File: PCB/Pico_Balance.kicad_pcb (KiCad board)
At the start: 2 copper layers, 100 x 52 mm, 42 parts, among them J1 XT60PW-M, J2 GPIO_Ext, J3 Conn_Motor0, J4 Conn_Motor1, J5 5V3A OUT, Q1 CSD17577Q3A, U1 BMI160, U2 DRV8876PWPR, U3 DRV8876PWPR, U4 LM74610QDGKRQ1, U5 LMR51430

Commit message: Refinements
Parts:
- U1: value BMI160 -> BMI323
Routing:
- net +3V3: track 200.9 -> 210.2 mm, vias 2 -> 3
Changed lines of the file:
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@@
 			)
 		)
-		(property "Value" "BMI160"
+		(property "Value" "BMI323"
 			(at 4.3375 0.45 270)
 			(unlocked yes)
@@
 		(embedded_fonts no)
 	)
+	(gr_line
+		(start 249 80)
+		(end 248.25 80.5)
+		(stroke
+			(width 0.2)
+			(type solid)
+		)
+		(layer "F.SilkS")
+	)
 	(gr_rect
 		(start 155.8 73)
@@
 		(layer "F.SilkS")
 	)
+	(gr_line
+		(start 245 80)
+		(end 249 80)
+		(stroke
+			(width 0.2)
+			(type solid)
+		)
+		(layer "F.SilkS")
+	)
 	(gr_rect
 		(start 155.8 114.6)
@@
 		(layer "F.SilkS")
 	)
+	(gr_line
+		(start 249 80)
+		(end 248.25 79.5)
+		(stroke
+			(width 0.2)
+			(type solid)
+		)
+		(layer "F.SilkS")
+	)
+	(gr_line
+		(start 245 76)
+		(end 245.5 76.75)
+		(stroke
+			(width 0.2)
+			(type solid)
+		)
+		(layer "F.SilkS")
+	)
+	(gr_circle
+		(center 245 80)
+		(end 245.5 80)
+		(stroke
+			(width 0.2)
+			(type solid)
+		)
+		(fill no)
+		(layer "F.SilkS")
+	)
+	(gr_line
+		(start 245 76)
+		(end 244.5 76.75)
+		(stroke
+			(width 0.2)
+			(type solid)
+		)
+		(layer "F.SilkS")
+	)
 	(gr_rect
 		(start 242.6 83.6)
-		(end 251 90.4)
+		(end 251 90.5)
 		(stroke
 			(width 0.2)
@@
 		(layer "F.SilkS")
 	)
+	(gr_line
+		(start 245 80)
+		(end 245 76)
+		(stroke
+			(width 0.2)
+			(type solid)
+		)
+		(layer "F.SilkS")
+	)
 	(gr_rect
 		(start 200.725 120.8)
@@
 		(cells
 			(table_cell "M+"
-				(start 171.95 73.25)
-				(end 169.3 76.8)
+				(start 171.95 73.725)
+				(end 169.3 77.275)
 				(margins 0.1 0.1 0.1 0.1)
 				(span 1 1)
@@
 						(thickness 0.15)
 					)
-					(justify left)
 				)
 			)
 			(table_cell "3V"
-				(start 169.3 73.25)
-				(end 166.8 76.8)
+				(start 169.3 73.725)
+				(end 166.8 77.275)
 				(margins 0.1 0.1 0.1 0.1)
 				(span 1 1)
@@
 						(thickness 0.15)
 					)
-					(justify left)
 				)
 			)
 			(table_cell "EA"
-				(start 166.8 73.25)
-				(end 164.4 76.8)
+				(start 166.8 73.725)
+				(end 164.4 77.275)
 				(margins 0.1 0.1 0.1 0.1)
 				(span 1 1)
@@
 						(thickness 0.15)
 					)
-					(justify left)
 				)
 			)
 			(table_cell "EB"
-				(start 164.4 73.25)
-				(end 161.6 76.8)
+				(start 164.4 73.725)
+				(end 161.6 77.275)
 				(margins 0.1 0.1 0.1 0.1)
 				(span 1 1)
@@
 						(thickness 0.15)
 					)
-					(justify left)
 				)
 			)
 			(table_cell "GND"
-				(start 161.6 73.25)
-				(end 159.4 76.8)
+				(start 161.6 73.725)
+				(end 159.4 77.275)
 				(margins 0.1 0.1 0.1 0.1)
 				(span 1 1)
@@
 						(thickness 0.15)
 					)
-					(justify left)
 				)
 			)
 			(table_cell "M-"
-				(start 159.4 73.25)
-				(end 156.8 76.8)
+				(start 159.4 73.725)
+				(end 156.8 77.275)
 				(margins 0.1 0.1 0.1 0.1)
 				(span 1 1)
@@
 						(thickness 0.15)
 					)
-					(justify left)
 				)
 			)
@@
 		(cells
 			(table_cell "M+"
-				(start 171.975 119.425)
-				(end 169.325 122.975)
+				(start 171.975 118.725)
+				(end 169.325 122.275)
 				(margins 0.1 0.1 0.1 0.1)
 				(span 1 1)
@@
 						(thickness 0.15)
 					)
-					(justify left)
 				)
 			)
 			(table_cell "3V"
-				(start 169.325 119.425)
-				(end 166.825 122.975)
+				(start 169.325 118.725)
+				(end 166.825 122.275)
 				(margins 0.1 0.1 0.1 0.1)
 				(span 1 1)
@@
 						(thickness 0.15)
 					)
-					(justify left)
 				)
 			)
 			(table_cell "EA"
-				(start 166.825 119.425)
-				(end 164.425 122.975)
+				(start 166.825 118.725)
+				(end 164.425 122.275)
 				(margins 0.1 0.1 0.1 0.1)
 				(span 1 1)
@@
 						(thickness 0.15)
 					)
-					(justify left)
 				)
 			)
 			(table_cell "EB"
-				(start 164.425 119.425)
-				(end 161.625 122.975)
+				(start 164.425 118.725)
+				(end 161.625 122.275)
 				(margins 0.1 0.1 0.1 0.1)
 				(span 1 1)
@@
 						(thickness 0.15)
 					)
-					(justify left)
 				)
 			)
 			(table_cell "GND"
-				(start 161.625 119.425)
-				(end 159.425 122.975)
+				(start 161.625 118.725)
+				(end 159.425 122.275)
 				(margins 0.1 0.1 0.1 0.1)
 				(span 1 1)
@@
 						(thickness 0.15)
 					)
-					(justify left)
 				)
 			)
 			(table_cell "M-"
-				(start 159.425 119.425)
-				(end 156.825 122.975)
+				(start 159.425 118.725)
+				(end 156.825 122.275)
 				(margins 0.1 0.1 0.1 0.1)
 				(span 1 1)
@@
 						(thickness 0.15)
 					)
-					(justify left)
 				)
 			)
@@
 	)
 	(segment
+		(start 243.4 88.4)
+		(end 242.848527 88.4)
+		(width 0.2)
+		(layer "F.Cu")
+		(net 9)
+	)
+	(segment
 		(start 219.001 72.601)
 		(end 174.599 72.601)
@@
 	)
 	(segment
+		(start 242.848527 88.4)
+		(end 242.048527 87.6)
+		(width 0.2)
+		(layer "F.Cu")
+		(net 9)
+	)
+	(segment
 		(start 245.1625 87.7175)
 		(end 245.1625 87.5625)
@@
 	)
 	(segment
+		(start 243.4 88.4)
+		(end 243.4 86.2355)
+		(width 0.2)
+		(layer "F.Cu")
+		(net 9)
+	)
+	(segment
 		(start 162.539 82.611)
 		(end 160.7 84.45)
@@
 	(segment
 		(start 243.4 89.48)
-		(end 243.4 86.2355)
+		(end 243.4 88.4)
 		(width 0.2)
 		(layer "F.Cu")
@@
 	)
 	(via
+		(at 242.048527 87.6)
+		(size 0.6)
+		(drill 0.3)
+		(layers "F.Cu" "B.Cu")
+		(net 9)
+	)
+	(via
 		(at 153.602 92.6)
 		(size 0.6)
@@
 	)
 	(segment
+		(start 238.648527 84.2)
+		(end 235.865 84.2)
+		(width 0.2)
+		(layer "B.Cu")
+		(net 9)
+	)
+	(segment
+		(start 242.048527 87.6)
+		(end 238.648527 84.2)
+		(width 0.2)
+		(layer "B.Cu")
+		(net 9)
+	)
+	(segment
 		(start 153.602 112.202)
 		(end 153.602 109.8)
@@
 	)
 	(segment
-		(start 246.789 94.389)
-		(end 240.6 88.2)
+		(start 244.601 103.601)
+		(end 244.601 92.201)
 		(width 0.2)
 		(layer "B.Cu")
@@
 	)
 	(segment
-		(start 245.6 86.4)
-		(end 243.8 88.2)
+		(start 247.94 119.28)
+		(end 246.789 118.129)
 		(width 0.2)
 		(layer "B.Cu")
@@
 	)
 	(segment
-		(start 246.789 118.129)
-		(end 246.789 94.389)
+		(start 245.6 86.4)
+		(end 243.8 88.2)
 		(width 0.2)
 		(layer "B.Cu")
@@
 	)
 	(segment
-		(start 247.94 119.28)
-		(end 246.789 118.129)
+		(start 244.601 92.201)
+		(end 240.6 88.2)
 		(width 0.2)
 		(layer "B.Cu")
@@
 	)
 	(segment
+		(start 246.789 105.789)
+		(end 244.601 103.601)
+		(width 0.2)
+		(layer "B.Cu")
+		(net 18)
+	)
+	(segment
 		(start 219.186 88.179)
 		(end 218.085 89.28)
@@
 	)
 	(segment
+		(start 246.789 118.129)
+		(end 246.789 105.789)
+		(width 0.2)
+		(layer "B.Cu")
+		(net 18)
+	)
+	(segment
 		(start 173.098 122.3)
 		(end 173 122.398)
@@
 	)
 	(group ""
+		(members "0e098a54-aab8-48f0-ad5a-1b8c5dcb6939" "3d4db691-04d1-4923-84a8-ca63cf973a07"
+			"4c652e14-a829-45d9-ae98-6ccd60f11574" "63e503f4-efba-4b57-b139-408cbbdc4a5a"
+			"90350472-ea7e-46d9-adf6-18d1887b5930" "97e5d2a3-c56d-46de-99b1-c52cc26e95a4"
+			"af4be8ed-c6e8-495a-9d4b-11de16a7dfe8"
+		)
+	)
+	(group ""

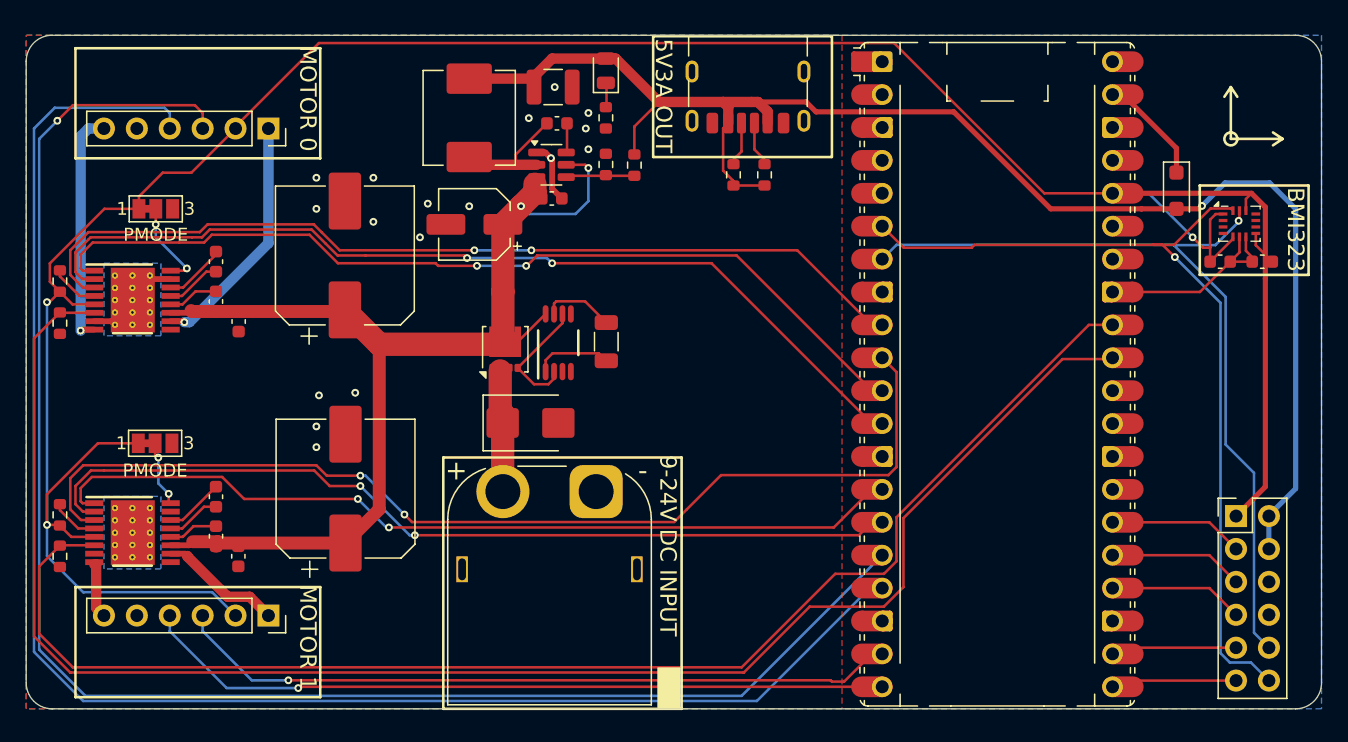
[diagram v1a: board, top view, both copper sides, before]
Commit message: minor silkscreen and drc error correction
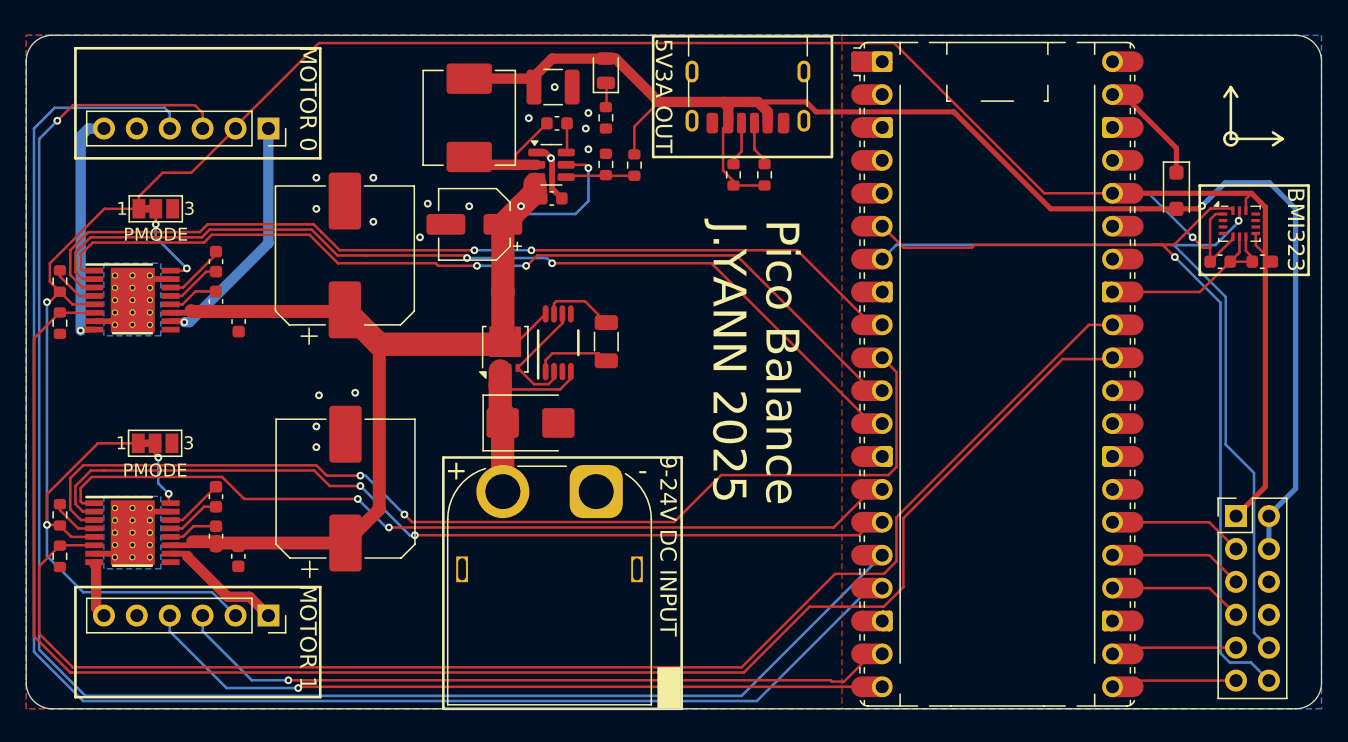
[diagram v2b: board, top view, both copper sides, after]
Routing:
- net Net-(D1-A1): track 9.41 -> 15.9 mm
- net GND: track 24.4 -> 27.8 mm
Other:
- board text added: "Pico Balance J.YANN 2025"
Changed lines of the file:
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@@
 		(pad "1" smd roundrect
 			(at -1.44 -0.97 90)
-			(size 0.63 0.5)
+			(size 0.63 0.33)
 			(layers "F.Cu" "F.Mask" "F.Paste")
 			(roundrect_rratio 0.25)
@@
 		(pad "2" smd roundrect
 			(at -1.44 -0.33 90)
-			(size 0.63 0.5)
+			(size 0.63 0.33)
 			(layers "F.Cu" "F.Mask" "F.Paste")
 			(roundrect_rratio 0.25)
@@
 		(pad "3" smd roundrect
 			(at -1.44 0.33 90)
-			(size 0.63 0.5)
+			(size 0.63 0.33)
 			(layers "F.Cu" "F.Mask" "F.Paste")
 			(roundrect_rratio 0.25)
@@
 		(pad "4" smd roundrect
 			(at -1.44 0.97 90)
-			(size 0.63 0.5)
+			(size 0.63 0.33)
 			(layers "F.Cu" "F.Mask" "F.Paste")
 			(roundrect_rratio 0.25)
@@
 		(pad "17" thru_hole circle
 			(at -1.35 -1.900001)
-			(size 0.499999 0.499999)
-			(drill 0.2032)
+			(size 0.5 0.5)
+			(drill 0.3)
 			(layers "*.Cu" "*.Mask")
 			(remove_unused_layers no)
@@
 		(pad "17" thru_hole circle
 			(at -1.35 -0.950001)
-			(size 0.499999 0.499999)
-			(drill 0.2032)
+			(size 0.5 0.5)
+			(drill 0.3)
 			(layers "*.Cu" "*.Mask")
 			(remove_unused_layers no)
@@
 		(pad "17" thru_hole circle
 			(at -1.35 0)
-			(size 0.499999 0.499999)
-			(drill 0.2032)
+			(size 0.5 0.5)
+			(drill 0.3)
 			(layers "*.Cu" "*.Mask")
 			(remove_unused_layers no)
@@
 		(pad "17" thru_hole circle
 			(at -1.35 0.950001)
-			(size 0.499999 0.499999)
-			(drill 0.2032)
+			(size 0.5 0.5)
+			(drill 0.3)
 			(layers "*.Cu" "*.Mask")
 			(remove_unused_layers no)
@@
 		(pad "17" thru_hole circle
 			(at -1.35 1.900001)
-			(size 0.499999 0.499999)
-			(drill 0.2032)
+			(size 0.5 0.5)
+			(drill 0.3)
 			(layers "*.Cu" "*.Mask")
 			(remove_unused_layers no)
@@
 		(pad "17" thru_hole circle
 			(at 0 -1.900001)
-			(size 0.499999 0.499999)
-			(drill 0.2032)
+			(size 0.5 0.5)
+			(drill 0.3)
 			(layers "*.Cu" "*.Mask")
 			(remove_unused_layers no)
@@
 		(pad "17" thru_hole circle
 			(at 0 -0.950001)
-			(size 0.499999 0.499999)
-			(drill 0.2032)
+			(size 0.5 0.5)
+			(drill 0.3)
 			(layers "*.Cu" "*.Mask")
 			(remove_unused_layers no)
@@
 		(pad "17" thru_hole circle
 			(at 0 0)
-			(size 0.499999 0.499999)
-			(drill 0.2032)
+			(size 0.5 0.5)
+			(drill 0.3)
 			(layers "*.Cu" "*.Mask")
 			(remove_unused_layers no)
@@
 		(pad "17" thru_hole circle
 			(at 0 0.950001)
-			(size 0.499999 0.499999)
-			(drill 0.2032)
+			(size 0.5 0.5)
+			(drill 0.3)
 			(layers "*.Cu" "*.Mask")
 			(remove_unused_layers no)
@@
 		(pad "17" thru_hole circle
 			(at 0 1.900001)
-			(size 0.499999 0.499999)
-			(drill 0.2032)
+			(size 0.5 0.5)
+			(drill 0.3)
 			(layers "*.Cu" "*.Mask")
 			(remove_unused_layers no)
@@
 		(pad "17" thru_hole circle
 			(at 1.35 -1.900001)
-			(size 0.499999 0.499999)
-			(drill 0.2032)
+			(size 0.5 0.5)
+			(drill 0.3)
 			(layers "*.Cu" "*.Mask")
 			(remove_unused_layers no)
@@
 		(pad "17" thru_hole circle
 			(at 1.35 -0.950001)
-			(size 0.499999 0.499999)
-			(drill 0.2032)
+			(size 0.5 0.5)
+			(drill 0.3)
 			(layers "*.Cu" "*.Mask")
 			(remove_unused_layers no)
@@
 		(pad "17" thru_hole circle
 			(at 1.35 0)
-			(size 0.499999 0.499999)
-			(drill 0.2032)
+			(size 0.5 0.5)
+			(drill 0.3)
 			(layers "*.Cu" "*.Mask")
 			(remove_unused_layers no)
@@
 		(pad "17" thru_hole circle
 			(at 1.35 0.950001)
-			(size 0.499999 0.499999)
-			(drill 0.2032)
+			(size 0.5 0.5)
+			(drill 0.3)
 			(layers "*.Cu" "*.Mask")
 			(remove_unused_layers no)
@@
 		(pad "17" thru_hole circle
 			(at 1.35 1.900001)
-			(size 0.499999 0.499999)
-			(drill 0.2032)
+			(size 0.5 0.5)
+			(drill 0.3)
 			(layers "*.Cu" "*.Mask")
 			(remove_unused_layers no)
@@
 		(pad "17" thru_hole circle
 			(at -1.35 -1.900001)
-			(size 0.499999 0.499999)
-			(drill 0.2032)
+			(size 0.5 0.5)
+			(drill 0.3)
 			(layers "*.Cu" "*.Mask")
 			(remove_unused_layers no)
@@
 		(pad "17" thru_hole circle
 			(at -1.35 -0.950001)
-			(size 0.499999 0.499999)
-			(drill 0.2032)
+			(size 0.5 0.5)
+			(drill 0.3)
 			(layers "*.Cu" "*.Mask")
 			(remove_unused_layers no)
@@
 		(pad "17" thru_hole circle
 			(at -1.35 0)
-			(size 0.499999 0.499999)
-			(drill 0.2032)
+			(size 0.5 0.5)
+			(drill 0.3)
 			(layers "*.Cu" "*.Mask")
 			(remove_unused_layers no)
@@
 		(pad "17" thru_hole circle
 			(at -1.35 0.950001)
-			(size 0.499999 0.499999)
-			(drill 0.2032)
+			(size 0.5 0.5)
+			(drill 0.3)
 			(layers "*.Cu" "*.Mask")
 			(remove_unused_layers no)
@@
 		(pad "17" thru_hole circle
 			(at -1.35 1.900001)
-			(size 0.499999 0.499999)
-			(drill 0.2032)
+			(size 0.5 0.5)
+			(drill 0.3)
 			(layers "*.Cu" "*.Mask")
 			(remove_unused_layers no)
@@
 		(pad "17" thru_hole circle
 			(at 0 -1.900001)
-			(size 0.499999 0.499999)
-			(drill 0.2032)
+			(size 0.5 0.5)
+			(drill 0.3)
 			(layers "*.Cu" "*.Mask")
 			(remove_unused_layers no)
@@
 		(pad "17" thru_hole circle
 			(at 0 -0.950001)
-			(size 0.499999 0.499999)
-			(drill 0.2032)
+			(size 0.5 0.5)
+			(drill 0.3)
 			(layers "*.Cu" "*.Mask")
 			(remove_unused_layers no)
@@
 		(pad "17" thru_hole circle
 			(at 0 0)
-			(size 0.499999 0.499999)
-			(drill 0.2032)
+			(size 0.5 0.5)
+			(drill 0.3)
 			(layers "*.Cu" "*.Mask")
 			(remove_unused_layers no)
@@
 		(pad "17" thru_hole circle
 			(at 0 0.950001)
-			(size 0.499999 0.499999)
-			(drill 0.2032)
+			(size 0.5 0.5)
+			(drill 0.3)
 			(layers "*.Cu" "*.Mask")
 			(remove_unused_layers no)
@@
 		(pad "17" thru_hole circle
 			(at 0 1.900001)
-			(size 0.499999 0.499999)
-			(drill 0.2032)
+			(size 0.5 0.5)
+			(drill 0.3)
 			(layers "*.Cu" "*.Mask")
 			(remove_unused_layers no)
@@
 		(pad "17" thru_hole circle
 			(at 1.35 -1.900001)
-			(size 0.499999 0.499999)
-			(drill 0.2032)
+			(size 0.5 0.5)
+			(drill 0.3)
 			(layers "*.Cu" "*.Mask")
 			(remove_unused_layers no)
@@
 		(pad "17" thru_hole circle
 			(at 1.35 -0.950001)
-			(size 0.499999 0.499999)
-			(drill 0.2032)
+			(size 0.5 0.5)
+			(drill 0.3)
 			(layers "*.Cu" "*.Mask")
 			(remove_unused_layers no)
@@
 		(pad "17" thru_hole circle
 			(at 1.35 0)
-			(size 0.499999 0.499999)
-			(drill 0.2032)
+			(size 0.5 0.5)
+			(drill 0.3)
 			(layers "*.Cu" "*.Mask")
 			(remove_unused_layers no)
@@
 		(pad "17" thru_hole circle
 			(at 1.35 0.950001)
-			(size 0.499999 0.499999)
-			(drill 0.2032)
+			(size 0.5 0.5)
+			(drill 0.3)
 			(layers "*.Cu" "*.Mask")
 			(remove_unused_layers no)
@@
 		(pad "17" thru_hole circle
 			(at 1.35 1.900001)
-			(size 0.499999 0.499999)
-			(drill 0.2032)
+			(size 0.5 0.5)
+			(drill 0.3)
 			(layers "*.Cu" "*.Mask")
 			(remove_unused_layers no)
@@
 		(layer "Edge.Cuts")
 	)
+	(gr_text "Pico Balance\nJ.YANN 2025"
+		(at 204.75 97.25 270)
+		(layer "F.SilkS" knockout)
+		(effects
+			(font
+				(size 2.54 2.54)
+				(thickness 0.4)
+			)
+			(justify bottom)
+		)
+	)
 	(gr_text "MOTOR 1"
 		(at 173 114.4 270)
@@
 	)
 	(segment
+		(start 163.150002 108.775002)
+		(end 161.825003 108.775002)
+		(width 0.45)
+		(layer "F.Cu")
+		(net 8)
+	)
+	(segment
+		(start 158.575 112.025001)
+		(end 158.85 112.300001)
+		(width 0.45)
+		(layer "F.Cu")
+		(net 8)
+	)
+	(segment
 		(start 246.65 89.13)
 		(end 246.1625 88.6425)
@@
 	)
 	(segment
+		(start 157.250001 112.025001)
+		(end 158.575 112.025001)
+		(width 0.45)
+		(layer "F.Cu")
+		(net 8)
+	)
+	(segment
 		(start 194.15 76)
 		(end 194.15 76.75)
@@
 	)
 	(segment
+		(start 161.825003 108.775002)
+		(end 161.55 108.499999)
+		(width 0.45)
+		(layer "F.Cu")
+		(net 8)
+	)
+	(segment
 		(start 244.95 89.48)
 		(end 242.61 91.82)
@@
 	)
 	(segment
+		(start 193.214377 99.341999)
+		(end 188.933499 99.341999)
+		(width 0.2)
+		(layer "F.Cu")
+		(net 55)
+	)
+	(segment
 		(start 188.8 105.5975)
 		(end 188.8 107.23)
@@
 	(segment
 		(start 188.5915 100.9915)
-		(end 188.5915 97.911)
+		(end 188.5915 99)
 		(width 1.8)
 		(layer "F.Cu")
@@
 		(layer "F.Cu")
 		(net 55)
+	)
+	(segment
+		(start 188.5915 99)
+		(end 188.5915 97.911)
+		(width 1.8)
+		(layer "F.Cu")
+		(net 55)
+	)
+	(segment
+		(start 194.047502 97.964999)
+		(end 194.047502 98.508874)
+		(width 0.2)
+		(layer "F.Cu")
+		(net 55)
+	)
+	(segment
+		(start 194.047502 98.508874)
+		(end 193.214377 99.341999)
+		(width 0.2)
+		(layer "F.Cu")
+		(net 55)
+	)
+	(segment
+		(start 188.933499 99.341999)
+		(end 188.5915 99)
+		(width 0.2)
+		(layer "F.Cu")
+		(net 55)
